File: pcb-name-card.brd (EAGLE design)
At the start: 84 x 53 mm, 8 parts, among them U1 3V, U2 3V

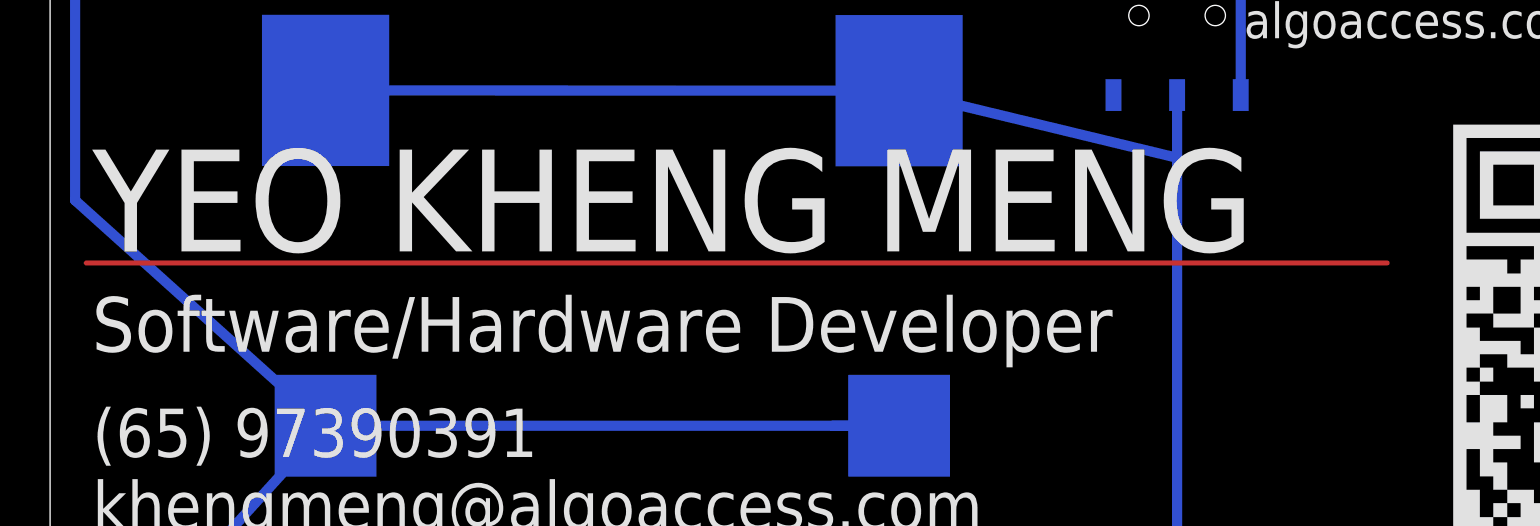
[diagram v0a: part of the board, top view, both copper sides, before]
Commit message: some text changes
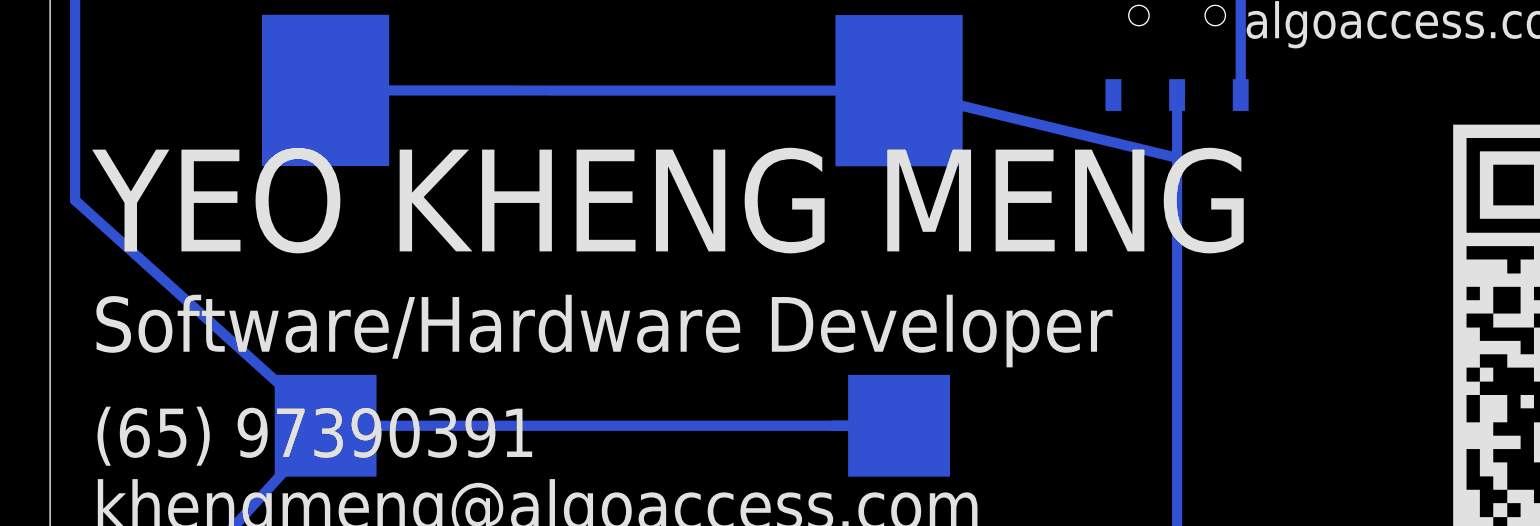
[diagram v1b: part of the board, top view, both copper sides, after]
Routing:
- net N$3: track 52.0 -> 0.00 mm
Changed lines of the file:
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@@
 <layer number="27" name="tValues" color="7" fill="1" visible="yes" active="yes"/>
 <layer number="28" name="bValues" color="7" fill="1" visible="yes" active="yes"/>
-<layer number="29" name="tStop" color="7" fill="3" visible="no" active="yes"/>
-<layer number="30" name="bStop" color="7" fill="6" visible="no" active="yes"/>
+<layer number="29" name="tStop" color="7" fill="3" visible="yes" active="yes"/>
+<layer number="30" name="bStop" color="7" fill="6" visible="yes" active="yes"/>
 <layer number="31" name="tCream" color="7" fill="4" visible="yes" active="yes"/>
 <layer number="32" name="bCream" color="7" fill="5" visible="yes" active="yes"/>
@@
 <text x="39.6" y="7.5" size="1.27" layer="22" font="vector" rot="MR90">White</text>
 <text x="39.6" y="42.3" size="1.27" layer="22" font="vector" rot="MR90">UV</text>
-<text x="37" y="9" size="1.27" layer="22" font="vector" rot="MR0">Hand-assembled by yours truly</text>
+<text x="37" y="8" size="1.27" layer="22" font="vector" rot="MR0">Hand-assembled by yours truly</text>
 </plain>
 <attributes>
@@
 <wire x1="45" y1="40.205309375" x2="45" y2="37.7" width="0.4064" layer="16"/>
 </signal>
-<signal name="N$3">
-<wire x1="1.44" y1="33.5" x2="53.39" y2="33.5" width="0.2" layer="1"/>
-</signal>
 </signals>

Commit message: shift some stuff forward by 1mm
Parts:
- moved U2 1.10 mm to (35.0, 27.0)
- moved SW1 1.00 mm to (46.0, 43.4)
- moved SW2 1.00 mm to (46.0, 9.92)
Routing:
- net N$7: track 246.2 -> 248.4 mm
- net N$9: track 95.6 -> 97.6 mm
- net N$5: track 25.7 -> 24.7 mm
- net N$4: track 26.1 -> 25.1 mm
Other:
- board text added: "Rev 4"
- board text removed: "Rev 3"
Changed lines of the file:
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@@
 <rectangle x1="53.547359375" y1="44.53955625" x2="54.187440625" y2="44.5700375" layer="22"/>
 <rectangle x1="53.66928125" y1="44.5700375" x2="54.096" y2="44.6005125" layer="22"/>
-<text x="49.771078125" y="39.7722" size="1.016" layer="22" font="vector" rot="MR270">Caution: Look away from LEDs
+<text x="51" y="39.7722" size="1.016" layer="22" font="vector" rot="MR270">Caution: Look away from LEDs
 before toggling the switches</text>
-<text x="24.21" y="19.06" size="0.8128" layer="22" font="vector" rot="MR0">Rev 3</text>
+<text x="25.21" y="19.06" size="0.8128" layer="22" font="vector" rot="MR0">Rev 4</text>
 <text x="47.671403125" y="42.473115625" size="1.4224" layer="21" font="vector">algoaccess.com</text>
 <rectangle x1="55.9391" y1="44.3959" x2="56.0915" y2="44.4213" layer="21"/>
@@
 <rectangle x1="56.0233" y1="38.9985" x2="81.4233" y2="39.0239" layer="21"/>
 <text x="37" y="6.1" size="1.016" layer="22" font="vector" rot="MR0">https://github.com/yeokm1/pcb-name-card</text>
-<text x="39.6" y="7.5" size="1.27" layer="22" font="vector" rot="MR90">White</text>
-<text x="39.6" y="42.3" size="1.27" layer="22" font="vector" rot="MR90">UV</text>
+<text x="40.5" y="7.5" size="1.27" layer="22" font="vector" rot="MR90">White</text>
+<text x="40.5" y="42.3" size="1.27" layer="22" font="vector" rot="MR90">UV</text>
 <text x="37" y="8" size="1.27" layer="22" font="vector" rot="MR0">Hand-assembled by yours truly</text>
 </plain>
@@
 <attribute name="COLOR" value="yellow" x="80.82315" y="32.81365" size="1.778" layer="28" rot="MR180" display="off"/>
 </element>
-<element name="U2" library="cr2032-large-side" package="CR2032-SMD" value="3V" x="33.9" y="27" smashed="yes" rot="MR90"/>
-<element name="SW1" library="Seeed-OPL-Switch" package="SW6-2.54-SMD-7.0X3.5X1.5MM" value="" x="45" y="43.380309375" smashed="yes" rot="MR90">
-<attribute name="MPN" value="MS-22C01" x="45" y="43.380309375" size="1.778" layer="28" rot="MR90" display="off"/>
-<attribute name="VALUE" x="40.301" y="41.475309375" size="0.889" layer="28" ratio="11" rot="MR90"/>
+<element name="U2" library="cr2032-large-side" package="CR2032-SMD" value="3V" x="35" y="27" smashed="yes" rot="MR90"/>
+<element name="SW1" library="Seeed-OPL-Switch" package="SW6-2.54-SMD-7.0X3.5X1.5MM" value="" x="46" y="43.380309375" smashed="yes" rot="MR90">
+<attribute name="MPN" value="MS-22C01" x="46" y="43.380309375" size="1.778" layer="28" rot="MR90" display="off"/>
+<attribute name="VALUE" x="41.301" y="41.475309375" size="0.889" layer="28" ratio="11" rot="MR90"/>
 </element>
-<element name="SW2" library="Seeed-OPL-Switch" package="SW6-2.54-SMD-7.0X3.5X1.5MM" value="" x="45" y="9.9229125" smashed="yes" rot="MR90">
-<attribute name="MPN" value="MS-22C01" x="45" y="9.9229125" size="1.778" layer="28" rot="MR90" display="off"/>
-<attribute name="VALUE" x="40.301" y="8.0179125" size="0.889" layer="28" ratio="11" rot="MR90"/>
+<element name="SW2" library="Seeed-OPL-Switch" package="SW6-2.54-SMD-7.0X3.5X1.5MM" value="" x="46" y="9.9229125" smashed="yes" rot="MR90">
+<attribute name="MPN" value="MS-22C01" x="46" y="9.9229125" size="1.778" layer="28" rot="MR90" display="off"/>
+<attribute name="VALUE" x="41.301" y="8.0179125" size="0.889" layer="28" ratio="11" rot="MR90"/>
 </element>
 <element name="LED2" library="led" package="PLCC2" value="White" x="80.938" y="19.9834" smashed="yes" rot="MR0">
@@
 <contactref element="SW2" pad="CH1A"/>
 <contactref element="R2" pad="1"/>
-<wire x1="47.54" y1="6.7479125" x2="66.794746875" y2="8.3" width="0.4064" layer="16"/>
+<wire x1="48.54" y1="6.7479125" x2="66.794746875" y2="8.3" width="0.4064" layer="16"/>
 <contactref element="SW2" pad="CH2A"/>
-<wire x1="47.54" y1="13.0979125" x2="47.54" y2="6.7479125" width="0.4064" layer="16"/>
+<wire x1="48.54" y1="13.0979125" x2="48.54" y2="6.7479125" width="0.4064" layer="16"/>
 </signal>
 <signal name="N$4">
 <contactref element="SW1" pad="CH2A"/>
 <contactref element="R1" pad="1"/>
-<wire x1="47.54" y1="46.555309375" x2="67.094746875" y2="44.1" width="0.4064" layer="16"/>
+<wire x1="48.54" y1="46.555309375" x2="67.094746875" y2="44.1" width="0.4064" layer="16"/>
 <contactref element="SW1" pad="CH1A"/>
-<wire x1="47.54" y1="46.555309375" x2="47.54" y2="40.205309375" width="0.4064" layer="16"/>
+<wire x1="48.54" y1="46.555309375" x2="48.54" y2="40.205309375" width="0.4064" layer="16"/>
 </signal>
 <signal name="N$11">
@@
 <contactref element="LED2" pad="C"/>
 <contactref element="LED1" pad="C"/>
-<wire x1="11" y1="27" x2="33.9" y2="27" width="0.4064" layer="16"/>
-<wire x1="31.241221875" y1="27" x2="33.9" y2="27" width="0.4064" layer="16"/>
+<wire x1="11" y1="27" x2="35" y2="27" width="0.4064" layer="16"/>
+<wire x1="31.241221875" y1="27" x2="35" y2="27" width="0.4064" layer="16"/>
 <wire x1="80.938" y1="18.2834" x2="71" y2="5" width="0.4064" layer="16"/>
 <wire x1="71" y1="5" x2="4" y2="5" width="0.4064" layer="16"/>
@@
 <contactref element="U2" pad="+$2"/>
 <contactref element="SW1" pad="COM1"/>
-<wire x1="11" y1="40.39" x2="33.9" y2="40.38" width="0.4064" layer="16"/>
-<wire x1="11" y1="13.62" x2="33.9" y2="13.61" width="0.4064" layer="16"/>
-<wire x1="33.9" y1="40.38" x2="45" y2="37.7" width="0.4064" layer="16"/>
-<wire x1="45" y1="37.7" x2="45" y2="15.6" width="0.4064" layer="16"/>
-<wire x1="45" y1="15.6" x2="33.9" y2="13.61" width="0.4064" layer="16"/>
-<wire x1="45" y1="13.0979125" x2="45" y2="15.6" width="0.4064" layer="16"/>
-<wire x1="45" y1="40.205309375" x2="45" y2="37.7" width="0.4064" layer="16"/>
+<wire x1="11" y1="40.39" x2="35" y2="40.38" width="0.4064" layer="16"/>
+<wire x1="11" y1="13.62" x2="35" y2="13.61" width="0.4064" layer="16"/>
+<wire x1="35" y1="40.38" x2="46" y2="37.7" width="0.4064" layer="16"/>
+<wire x1="46" y1="37.7" x2="46" y2="15.6" width="0.4064" layer="16"/>
+<wire x1="46" y1="15.6" x2="35" y2="13.61" width="0.4064" layer="16"/>
+<wire x1="46" y1="13.0979125" x2="46" y2="15.6" width="0.4064" layer="16"/>
+<wire x1="46" y1="40.205309375" x2="46" y2="37.7" width="0.4064" layer="16"/>
 </signal>
 </signals>

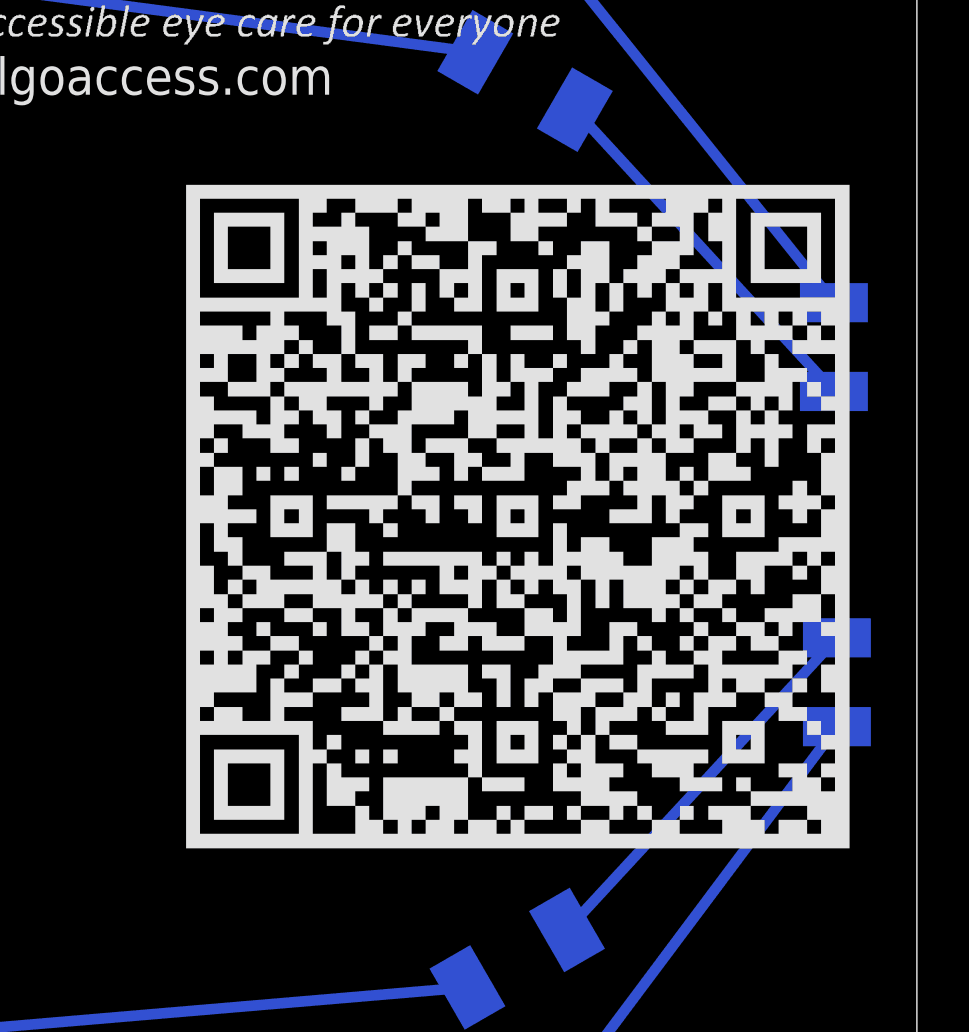
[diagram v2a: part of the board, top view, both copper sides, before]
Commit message: top square around QR code
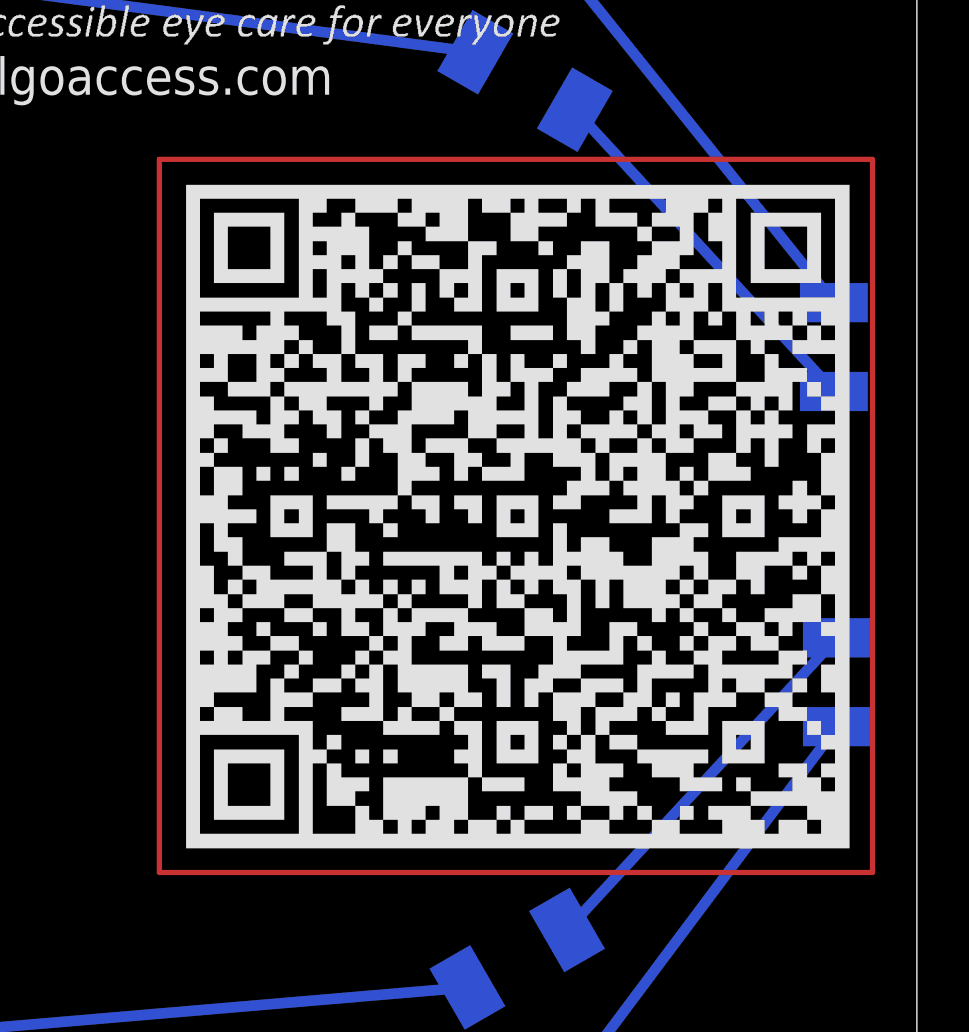
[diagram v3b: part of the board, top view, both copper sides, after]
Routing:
- net N$3: track 0.00 -> 109.2 mm
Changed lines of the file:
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@@
 <layer number="19" name="Unrouted" color="6" fill="1" visible="yes" active="yes"/>
 <layer number="20" name="Dimension" color="15" fill="1" visible="yes" active="yes"/>
-<layer number="21" name="tPlace" color="7" fill="1" visible="no" active="yes"/>
+<layer number="21" name="tPlace" color="7" fill="1" visible="yes" active="yes"/>
 <layer number="22" name="bPlace" color="7" fill="1" visible="yes" active="yes"/>
 <layer number="23" name="tOrigins" color="15" fill="1" visible="yes" active="yes"/>
@@
 <wire x1="46" y1="40.205309375" x2="46" y2="37.7" width="0.4064" layer="16"/>
 </signal>
+<signal name="N$3">
+<wire x1="55" y1="40" x2="82.3" y2="40" width="0.2" layer="1"/>
+<wire x1="82.3" y1="40" x2="82.3" y2="12.7" width="0.2" layer="1"/>
+<wire x1="82.3" y1="12.7" x2="55" y2="12.7" width="0.2" layer="1"/>
+<wire x1="55" y1="12.7" x2="55" y2="40" width="0.2" layer="1"/>
+</signal>
 </signals>
